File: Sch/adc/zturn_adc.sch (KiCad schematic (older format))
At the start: 0 parts

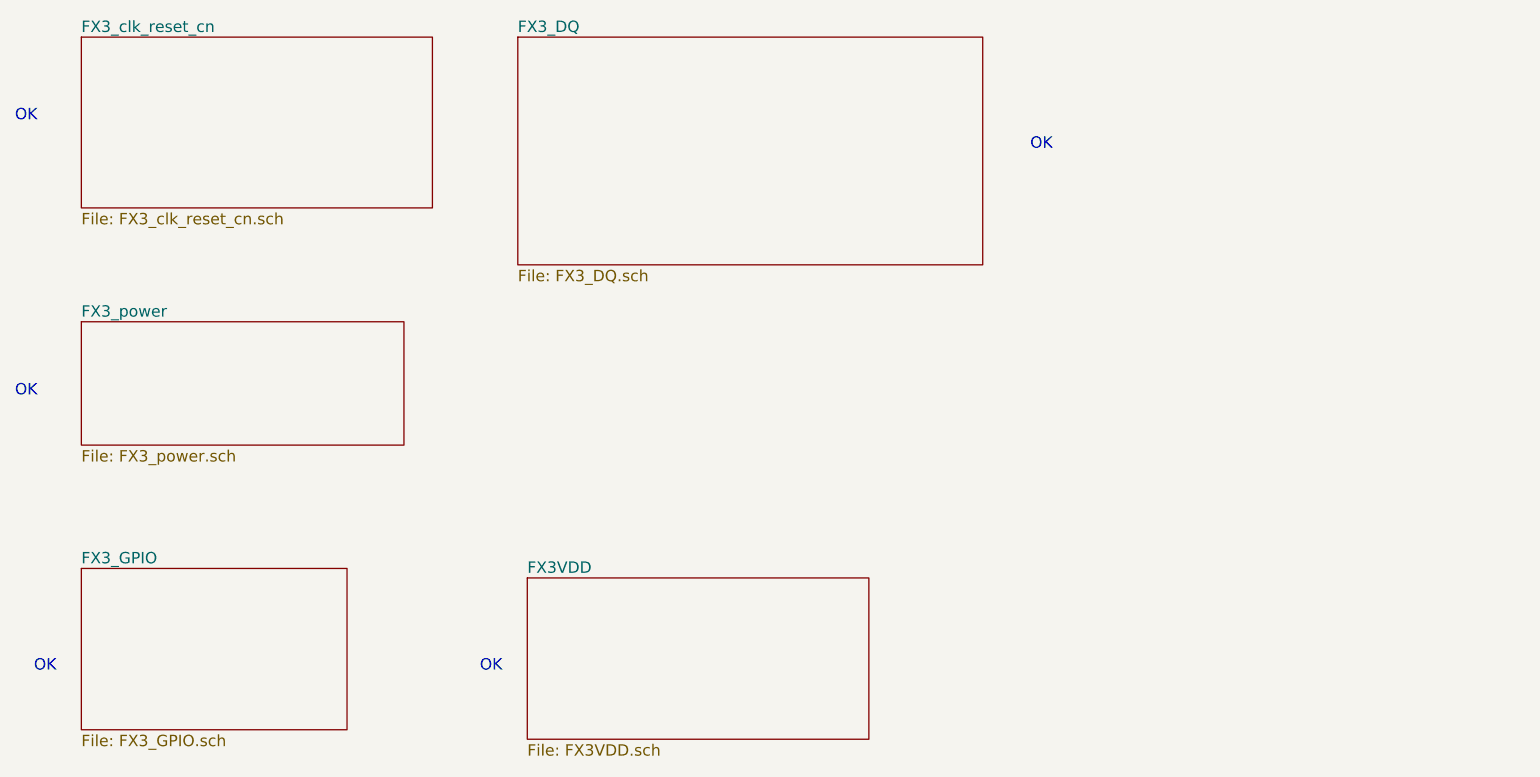
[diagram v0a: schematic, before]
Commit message: separate FX3 and ADC
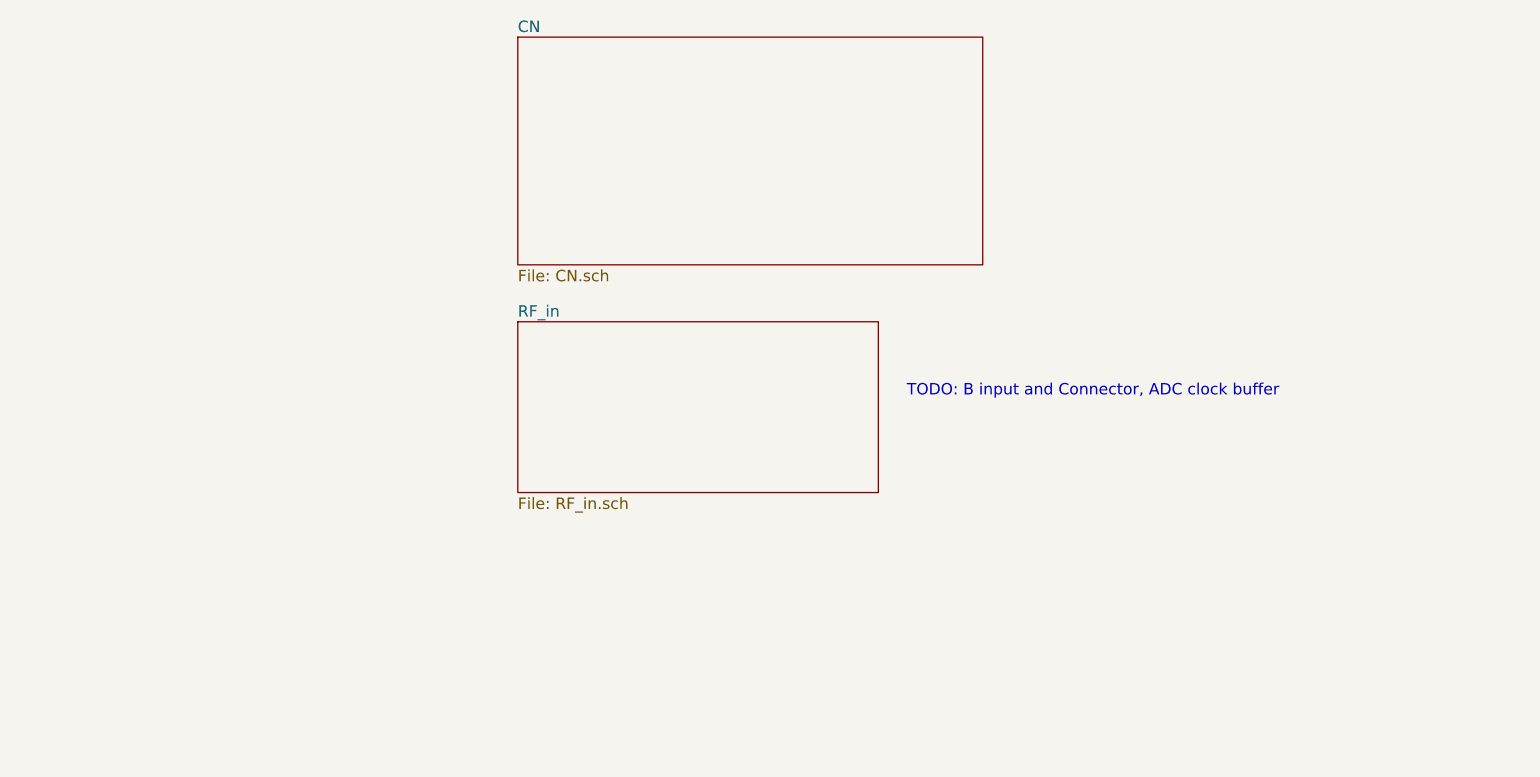
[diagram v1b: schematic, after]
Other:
- note added: "TODO: B input and Connector, ADC clock buffer"
- note removed: "OK"
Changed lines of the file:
@@
 $Descr A4 11693 8268
 encoding utf-8
-Sheet 1 6
+Sheet 1 3
 Title ""
 Date ""
@@
 $EndDescr
 $Sheet
-S 1750 1650 1850 900
-U 589ADF9D
-F0 "FX3_clk_reset_cn" 60
-F1 "FX3_clk_reset_cn.sch" 60
+S 4050 1650 2450 1200
+U 58A0A991
+F0 "CN" 60
+F1 "CN.sch" 60
 $EndSheet
 $Sheet
-S 1750 3150 1700 650
-U 58A06B55
-F0 "FX3_power" 60
-F1 "FX3_power.sch" 60
+S 4050 3150 1900 900
+U 58A1C0F3
+F0 "RF_in" 60
+F1 "RF_in.sch" 60
 $EndSheet
-$Sheet
-S 4050 1650 2450 1200
-U 58A0A991
-F0 "FX3_DQ" 60
-F1 "FX3_DQ.sch" 60
-$EndSheet
-$Sheet
-S 1750 4450 1400 850
-U 58A517F2
-F0 "FX3_GPIO" 60
-F1 "FX3_GPIO.sch" 60
-$EndSheet
-Text Notes 1500 5000 0    60   ~ 0
-OK
-Text Notes 1400 2100 0    60   ~ 0
-OK
-$Sheet
-S 4100 4500 1800 850
-U 58A458E3
-F0 "FX3VDD" 60
-F1 "FX3VDD.sch" 60
-$EndSheet
-Text Notes 3850 5000 0    60   ~ 0
-OK
-Text Notes 1400 3550 0    60   ~ 0
-OK
-Text Notes 6750 2250 0    60   ~ 0
-OK
+Text Notes 6100 3550 0    60   ~ 0
+TODO: B input and Connector, ADC clock buffer
 $EndSCHEMATC

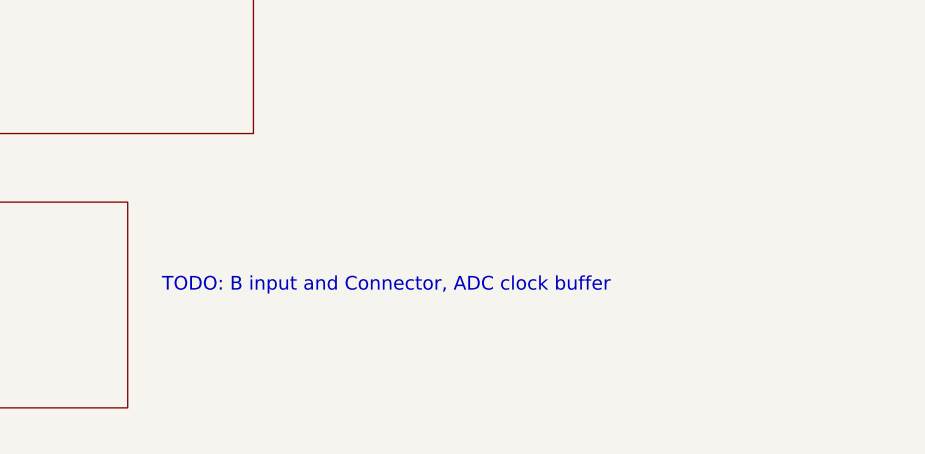
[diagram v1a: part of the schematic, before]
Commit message: Add resistors for ADC out
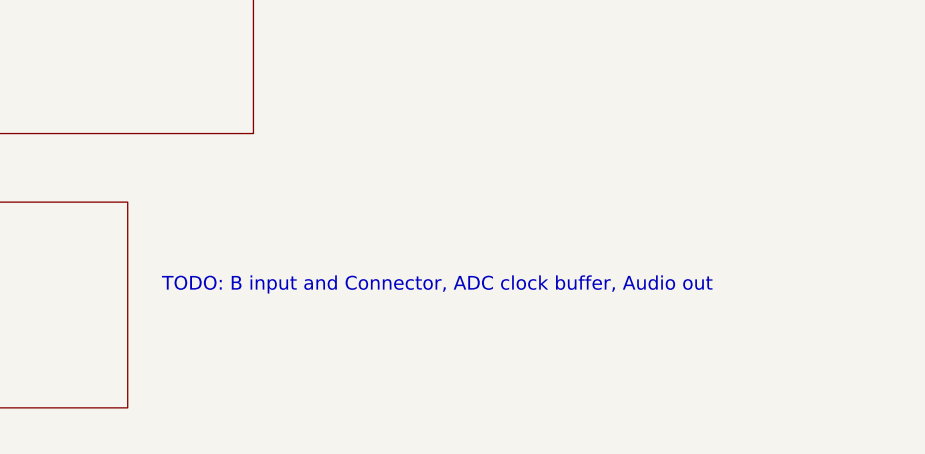
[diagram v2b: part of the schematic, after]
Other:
- note added: "TODO: B input and Connector, ADC clock buffer, Audio out"
- note removed: "TODO: B input and Connector, ADC clock buffer"
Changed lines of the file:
@@
 $EndSheet
 Text Notes 6100 3550 0    60   ~ 0
-TODO: B input and Connector, ADC clock buffer
+TODO: B input and Connector, ADC clock buffer, Audio out
 $EndSCHEMATC

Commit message: Add B-ch of the ADC
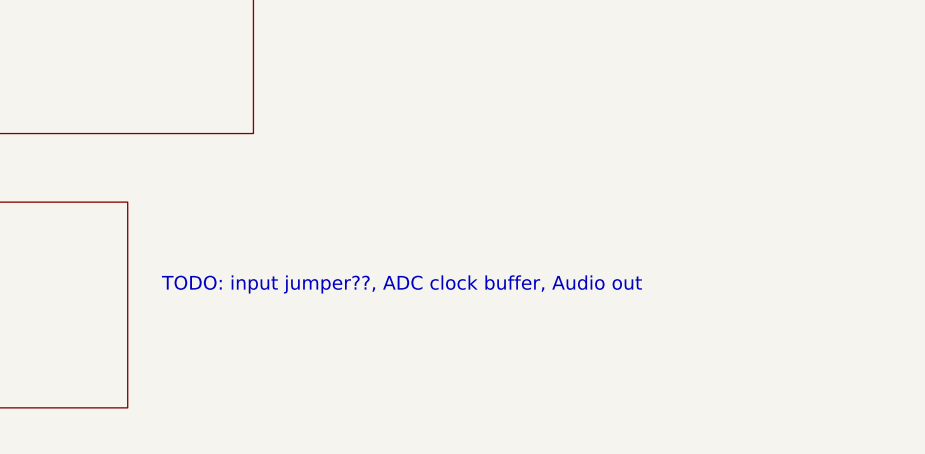
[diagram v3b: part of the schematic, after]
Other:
- note added: "TODO: input jumper??, ADC clock buffer, Audio out"
- note removed: "TODO: B input and Connector, ADC clock buffer, Audio out"
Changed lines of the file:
@@
 $EndSheet
 Text Notes 6100 3550 0    60   ~ 0
-TODO: B input and Connector, ADC clock buffer, Audio out
+TODO: input jumper??, ADC clock buffer, Audio out
 $EndSCHEMATC

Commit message: Almost finished except Audio
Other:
- note added: "TODO: Audio out"
- note removed: "TODO: input jumper??, ADC clock buffer, Audio out"
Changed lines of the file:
@@
 $EndSheet
 Text Notes 6100 3550 0    60   ~ 0
-TODO: input jumper??, ADC clock buffer, Audio out
+TODO: Audio out
 $EndSCHEMATC

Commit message: DAC in progress
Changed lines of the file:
@@
 $Descr A4 11693 8268
 encoding utf-8
-Sheet 1 3
+Sheet 1 4
 Title ""
 Date ""
@@
 F1 "RF_in.sch" 60
 $EndSheet
-Text Notes 6100 3550 0    60   ~ 0
+Text Notes 6100 4600 0    60   ~ 0
 TODO: Audio out
+$Sheet
+S 4100 4450 1850 800
+U 58A92E28
+F0 "AudioDAC" 60
+F1 "AudioDAC.sch" 60
+$EndSheet
 $EndSCHEMATC

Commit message: Schematics done
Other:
- note removed: "TODO: Audio out"
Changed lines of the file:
@@
 F1 "RF_in.sch" 60
 $EndSheet
-Text Notes 6100 4600 0    60   ~ 0
-TODO: Audio out
 $Sheet
 S 4100 4450 1850 800
